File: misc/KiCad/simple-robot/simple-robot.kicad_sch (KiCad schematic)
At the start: 54 parts, among them M3 Motor_Servo, U1 Pico2

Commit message: Upgrade KiCad project and schematic files
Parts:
- removed BATT1: Conn_01x02_Pin, Connector_PinHeader_2.54mm:PinHeader_1x02_P2.54mm_Vertical, symbol Connector:Conn_01x02_Pin
- removed C2: 220uF_10V, Capacitor_THT:CP_Radial_D6.3mm_P2.50mm, symbol PCM_SL_Capacitors:220uF_10V
- removed DBG1, IRL1, IRR1, SERVO1: Conn_01x03_Pin, Connector_PinHeader_2.54mm:PinHeader_1x03_P2.54mm_Vertical, symbol Connector:Conn_01x03_Pin
- removed ENCA1, ENCB1, HC-SRo4: Conn_01x04_Pin, Connector_PinHeader_2.54mm:PinHeader_1x04_P2.54mm_Vertical, symbol Connector:Conn_01x04_Pin
- removed EncoderA1, EncoderB1: ~, symbol common-hobby-things:Hall-effect_encoder
- removed HC-SR04-1: ~, symbol common-hobby-things:HC-SR04
- removed IMU1: ~, common-hobby-things:MPU 9265 IMU carrier board, symbol common-hobby-things:GY-9250_9-Axis
- removed IR_Sensor_Left1, IR_Sensor_Right1: ~, symbol common-hobby-things:IR_Proximity_Sensor
- removed M3: Motor_Servo, symbol Motor:Motor_Servo
- removed MA1, MB1: Motor_DC, symbol Motor:Motor_DC
- removed MOTA1, MOTB1: ~, Connector_PinHeader_2.54mm:PinHeader_1x02_P2.54mm_Vertical, symbol Connector:Conn_01x02_Pin
- removed S5V1: ~, common-hobby-things:Pololu step-up converter 2.5-5.5V in 5V out, symbol common-hobby-things:step-up-converter_5V
- removed S6V1: ~, common-hobby-things:Pololu step-up converter 2.5-5.5V in 6V out, symbol common-hobby-things:step-up-converter_6V
- removed TPENCA1, TPENCB1, TPGND1, TPGND2, TPSCL1, TPSDA1: Conn_01x01_Pin, Connector_PinHeader_2.54mm:PinHeader_1x01_P2.54mm_Vertical, symbol Connector:Conn_01x01_Pin
- added B1: LM2596 Module, symbol common-hobby-things:LM2596_Module
- added C16, C2: 100nF_Ceramic, Capacitor_THT:C_Disc_D5.0mm_W2.5mm_P2.50mm, symbol PCM_SL_Capacitors:100nF_Ceramic
- added C7: 220uF, Capacitor_THT:CP_Radial_D6.3mm_P2.50mm, symbol Device:C_Polarized
- added J1: MotLA, Connector_JST:JST_PH_B2B-PH-K_1x02_P2.00mm_Vertical, symbol PCM_SL_Connectors:JST_02
- added J10: Screw_Terminal_2_P5.00mm, TerminalBlock_Phoenix:TerminalBlock_Phoenix_PT-1,5-2-5.0-H_1x02_P5.00mm_Horizontal, symbol PCM_SL_Screw_Terminal:Screw_Terminal_2_P5.00mm
- added J2: MotLB, Connector_JST:JST_PH_B2B-PH-K_1x02_P2.00mm_Vertical, symbol PCM_SL_Connectors:JST_02
- added J4: MotRA, Connector_JST:JST_PH_B2B-PH-K_1x02_P2.00mm_Vertical, symbol PCM_SL_Connectors:JST_02
- added J5: MotRB, Connector_JST:JST_PH_B2B-PH-K_1x02_P2.00mm_Vertical, symbol PCM_SL_Connectors:JST_02
- added J6: ENC_LF, Connector_JST:JST_PH_B3B-PH-K_1x03_P2.00mm_Vertical, symbol PCM_SL_Connectors:JST_03
- added J7: ENC_LR, Connector_JST:JST_PH_B3B-PH-K_1x03_P2.00mm_Vertical, symbol PCM_SL_Connectors:JST_03
- added J8: ENC_RF, Connector_JST:JST_PH_B3B-PH-K_1x03_P2.00mm_Vertical, symbol PCM_SL_Connectors:JST_03
- added J9: ENC_RR, Connector_JST:JST_PH_B3B-PH-K_1x03_P2.00mm_Vertical, symbol PCM_SL_Connectors:JST_03
- added LS_3: Level Shifter, common-hobby-things:Level shifter 4 bi-dir, symbol common-hobby-things:level-shifter
- added MD2: RightTrack, common-hobby-things:TB6612FNG motor driver carrier, symbol common-hobby-things:TB6612FNG motor driver carrier
- added P1: Port Expander, symbol common-hobby-things:PCA9555
- C1: value 470uF -> 220uF
- C17: value 220uF_10V -> 10uF_10V
- LS_1, LS_2: value ~ -> Level Shifter
- MD1: value ~ -> LeftTrack
- R1: value ~ -> RF Receiver
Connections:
- net +3V8 is gone; now on net +5V: U1.39 (VSYS)
- net GND: now also C11.2, C12.2, C9.1, MD1.16 (GND), B1.2 (IN-), B1.4 (OUT-), C16.2, C2.1, C7.2, J10.2 (BAT-), J6.2 (GND), J7.2 (GND), J8.2 (GND), J9.2 (GND), LS_3.10 (GND), LS_3.4 (GND), MD2.1 (GND), MD2.16 (GND), MD2.8 (GND), P1.12 (GND), P1.2 (A1), P1.3 (A2); no longer C11.1, C12.1, C9.2
- net at LS_2.7 (HV1): now also J6.3 (SIG)
- net +3V3: now reaches C15.1, C4.1, C6.2, C8.1, LS_1.3 (LV), LS_2.3 (LV), MD1.2 (VCC), OLED1.2 (VCC), U1.36 (3V3)
- net +3V3: now also C9.2, MD2.2 (VCC), P1.21 (A0), P1.24 (V); no longer C14.1
- net +5V: now reaches C10.1, C13.1, C17.1, C3.1, C5.1, LS_1.9 (HV), LS_2.9 (HV), R1.2 (5V)
- net +5V: now also C11.1, C12.1, C14.1, B1.3 (OUT+), C16.1, C2.2, J6.1 (VCC), J7.1 (VCC), J8.1 (VCC), J9.1 (VCC); no longer C11.2, C12.2, C9.1
- net at R2.1: no longer U1.4 (GPIO2)
- net I2C SCL: now reaches U1.16 (GPIO12)
- net I2C SCL: now also OLED1.3 (SCL), P1.22 (SCL); no longer OLED1.4 (SDA)
- net +VBAT: now reaches C1.1, MD1.7 (VMOT)
- net +VBAT: now also B1.1 (IN+), C7.1, J10.1 (BAT+), MD2.7 (VMOT)
- net at MD1.3 (A01): now also J1.2 (-)
- net at MD1.4 (A02): now also J1.1 (+)
- net M_LF_PWM: now reaches U1.1 (GPIO0)
- net M_LF_PWM: now also MD1.9 (PWMA)
- net M_LR_PWM: now reaches U1.2 (GPIO1)
- net M_LR_PWM: now also MD1.15 (PWMB)
- net at R3.1: no longer U1.6 (GPIO4)
- net LMOT_F_REV: now reaches MD1.10 (AIN2)
- net LMOT_F_REV: now also P1.5 (P01); no longer U1.26 (GPIO20)
- net ENC_LR: now reaches U1.27 (GPIO21)
- net ENC_LR: now also LS_2.2 (LV2); no longer MD1.11 (AIN1)
- net at U1.29 (GPIO22): no longer MD1.12 (STBY)
- net at U1.25 (GPIO19): no longer MD1.13 (BIN1)
- net at U1.24 (GPIO18): no longer MD1.14 (BIN2)
- net ENC_RR: now reaches U1.32 (GPIO27_ADC1)
- net ENC_RR: now also LS_2.6 (LV4); no longer MD1.15 (PWMB)
- net at MD1.5 (B02): now also J2.1 (+)
- net at MD1.6 (B01): now also J2.2 (-)
- net at U1.34 (GPIO28_ADC2): no longer MD1.9 (PWMA)
- net at LS_2.8 (HV2): now also J7.3 (SIG)
- net ENC_LF: now reaches LS_2.1 (LV1)
- net ENC_LF: now also U1.10 (GPIO7); no longer U1.12 (GPIO9)
- net at LS_2.11 (HV3): now also J8.3 (SIG)
- net at LS_2.12 (HV4): now also J9.3 (SIG)
- net at U1.19 (GPIO14): no longer LS_2.5 (LV3)
- net at U1.20 (GPIO15): no longer LS_2.6 (LV4)
- net I2C SDA: now reaches U1.17 (GPIO13)
- net I2C SDA: now also OLED1.4 (SDA), P1.23 (SDA); no longer OLED1.3 (SCL)
- net at U1.22 (GPIO17): no longer LS_1.1 (LV1)
- net at U1.15 (GPIO11): no longer LS_1.2 (LV2)
- net at U1.21 (GPIO16): no longer LS_1.5 (LV3)
- net at U1.14 (GPIO10): no longer LS_1.6 (LV4)
- net M_RR_PWM: now reaches U1.5 (GPIO3)
- net M_RR_PWM: now also MD2.15 (PWMB)
- new net: J4.1 (+), MD2.4 (A02)
- new net: J4.2 (-), MD2.3 (A01)
- new net: J5.1 (+), MD2.5 (B02)
- new net: J5.2 (-), MD2.6 (B01)
- new net ENC_RF: LS_2.5 (LV3), U1.12 (GPIO9)
- new net LMOT_F_FWD: MD1.11 (AIN1), P1.4 (P00)
- new net LMOT_R_FWD: MD1.13 (BIN1), P1.6 (P02)
- new net LMOT_R_REV: MD1.14 (BIN2), P1.7 (P03)
- new net LMOT_STB: MD1.12 (STBY), P1.17 (P14)
- new net M_RF_PWM: MD2.9 (PWMA), U1.4 (GPIO2)
- new net PE_INT: P1.1 (INT), U1.26 (GPIO20)
- new net RC_A: LS_1.6 (LV4), P1.13 (P10)
- new net RC_B: LS_1.5 (LV3), P1.14 (P11)
- new net RC_C: LS_1.2 (LV2), P1.15 (P12)
- new net RC_D: LS_1.1 (LV1), P1.16 (P13)
- new net RMOT_F_FWD: MD2.11 (AIN1), P1.8 (P04)
- new net RMOT_F_REV: MD2.10 (AIN2), P1.9 (P05)
- new net RMOT_R_FWD: MD2.13 (BIN1), P1.10 (P06)
- new net RMOT_R_REV: MD2.14 (BIN2), P1.11 (P07)
- new net RMOT_STB: MD2.12 (STBY), P1.18 (P15)
- no-connect marks 13 -> 11
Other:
- note added: "Controller"
- note added: "Encoders"
- note added: "Motor Drivers"
- note added: "Mounting Holes"
- note added: "OLED"
- note added: "Port Expander"
- note added: "Power"
- note added: "RF Receiver"
- note added: "Status LED"
- moved on the sheet: C1, C13, C14, C15, C17, C3, C5, C6, C8, D3, H1, H2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

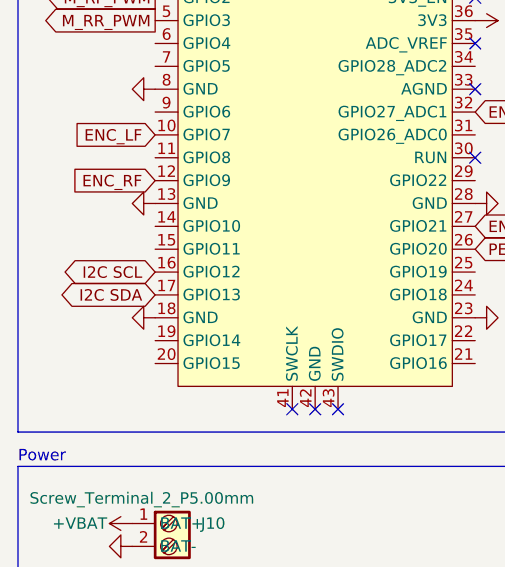
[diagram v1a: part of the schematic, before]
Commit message: Use SCL/SDA names for I2C and update schematic
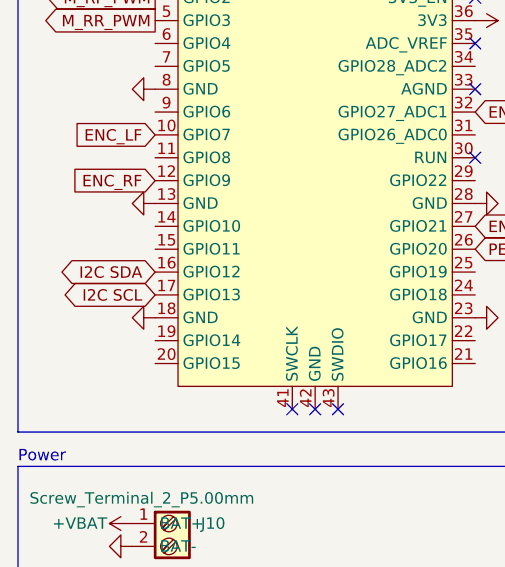
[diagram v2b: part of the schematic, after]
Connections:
- net I2C SCL: now also U1.17 (GPIO13); no longer U1.16 (GPIO12)
- net I2C SDA: now also U1.16 (GPIO12); no longer U1.17 (GPIO13)
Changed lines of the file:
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@@
+		)
+	)
+	(global_label "I2C SDA"
+		(shape bidirectional)
+		(at 30.48 60.96 180)
+		(effects
+			(font
+				(size 1.27 1.27)
+			)
+			(justify right)
+		)
+		(property "Intersheetrefs" "${INTERSHEET_REFS}"
+			(at 30.48 60.96 0)
+			(effects
+				(font
+					(size 1.27 1.27)
+				)
+				(hide yes)
+			)
 		)
 	)
@@
 		)
 	)
+	(global_label "I2C SCL"
+		(shape bidirectional)
+		(at 30.48 63.5 180)
+		(effects
+			(font
+				(size 1.27 1.27)
+			)
+			(justify right)
+		)
+		(property "Intersheetrefs" "${INTERSHEET_REFS}"
+			(at 30.48 63.5 0)
+			(effects
+				(font
+					(size 1.27 1.27)
+				)
+				(hide yes)
+			)
+		)
+	)
 	(global_label "RC_C"
 		(shape output)
@@
 			(effects
 				(font
-					(size 1.27 1.27)
-				)
-				(hide yes)
-			)
-		)
-	)
-	(global_label "I2C SDA"
-		(shape bidirectional)
-		(at 30.48 63.5 180)
-		(effects
-			(font
-				(size 1.27 1.27)
-			)
-			(justify right)
-		)
-		(property "Intersheetrefs" "${INTERSHEET_REFS}"
-			(at 30.48 63.5 0)
-			(effects
-				(font
-					(size 1.27 1.27)
-				)
-				(hide yes)
-			)
-		)
-	)
-	(global_label "I2C SCL"
-		(shape bidirectional)
-		(at 30.48 60.96 180)
-		(effects
-			(font
-				(size 1.27 1.27)
-			)
-			(justify right)
-		)
-		(property "Intersheetrefs" "${INTERSHEET_REFS}"
-			(at 30.48 60.96 0)
-			(effects
-				(font

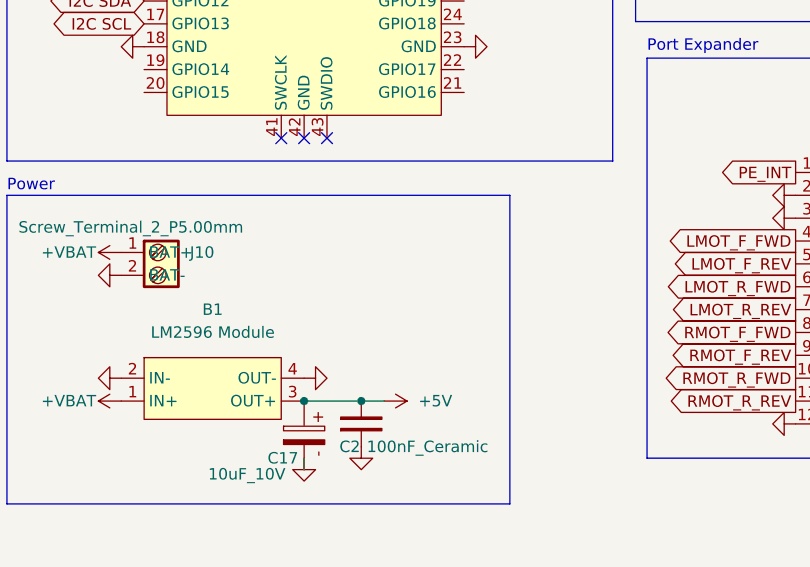
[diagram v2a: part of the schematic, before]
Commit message: Add 4700uF cap, 20k resistor and power symbols
Add schematic symbols and instances for C18 (4700uF_16V) and R4 (20k).
Add power symbols GND and +VBAT (+4V) plus corresponding wires and
junctions.
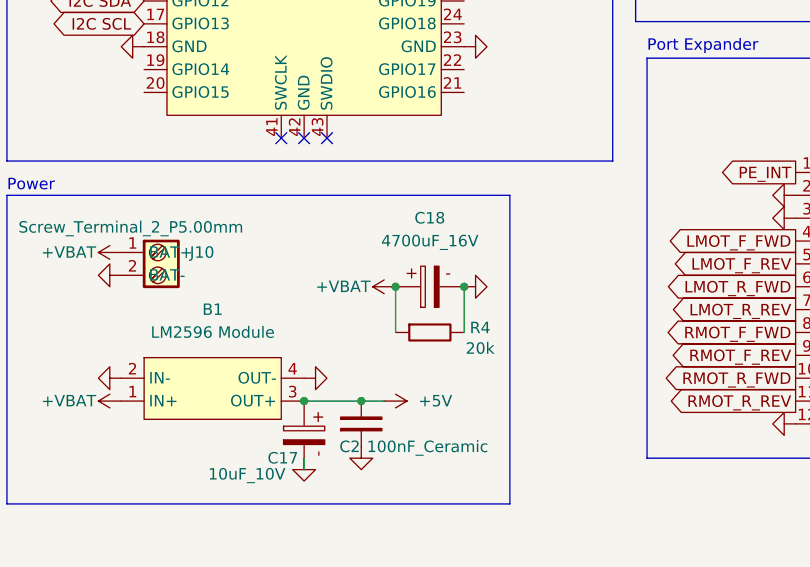
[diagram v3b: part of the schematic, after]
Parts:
- added C18: 4700uF_16V, Capacitor_THT:CP_Radial_D16.0mm_P7.50mm, symbol PCM_SL_Capacitors:4700uF_16V
- added R4: 20k, Resistor_THT:R_Axial_DIN0207_L6.3mm_D2.5mm_P10.16mm_Horizontal, symbol PCM_SL_Resistors:20k
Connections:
- net +VBAT: now also C18.1, R4.1
- net GND: now also C18.2, R4.2

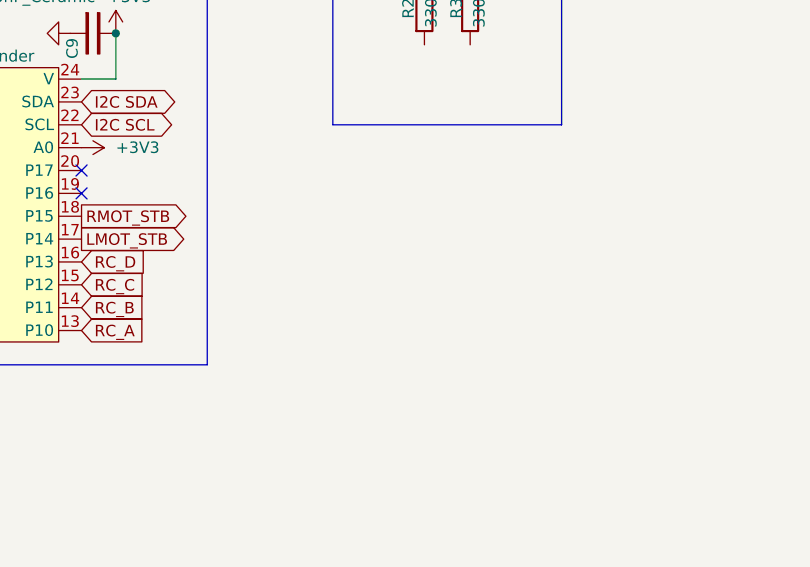
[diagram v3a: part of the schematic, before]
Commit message: Add I2C pull-up resistors and labels
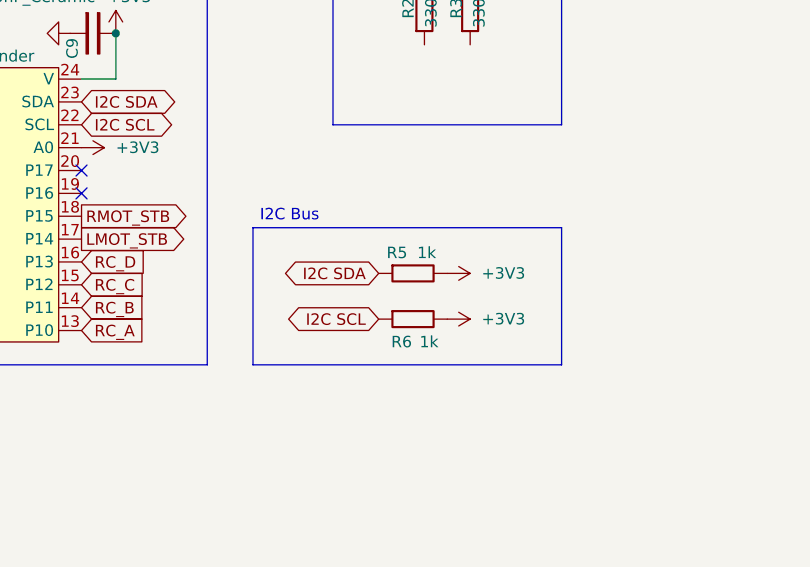
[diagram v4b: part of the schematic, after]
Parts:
- added R5, R6: 1k, Resistor_THT:R_Axial_DIN0207_L6.3mm_D2.5mm_P10.16mm_Horizontal, symbol PCM_SL_Resistors:1k
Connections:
- net +3V3: now also R5.2, R6.2
- net I2C SCL: now also R6.1
- net I2C SDA: now also R5.1
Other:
- note added: "I2C Bus"

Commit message: Upgrade KiCad project and refresh footprints
Refresh fp-info-cache with new battery and switch footprints.
Convert PCB to newer KiCad generator/version and update layers,
net names, footprint UUIDs and component positions.
Adjust plot/export and soldermask settings, and tenting.
Update project preferences and DRC/teardrop rules.
Bump schematic date and revision.
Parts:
- B1: footprint (none) -> common-hobby-things:LM2596_Module
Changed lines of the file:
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@@
 	(title_block
 		(title "simple-robot")
-		(date "2026-01-14")
-		(rev "3")
+		(date "2026-01-26")
+		(rev "4")
 		(company "Rafael Koch")
 	)
@@
 			)
 		)
-		(property "Footprint" ""
+		(property "Footprint" "common-hobby-things:LM2596_Module"
 			(at 38.1 99.06 0)
 			(effects
